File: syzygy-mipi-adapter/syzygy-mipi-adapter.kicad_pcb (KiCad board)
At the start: 4 copper layers, 45 x 70 mm, 67 parts, among them J1 Conn_02x06_Odd_Even, J10 501951-2230, J2 SYZYGY_STD, J3 Conn_01x02, J5 SM03B-SRSS-TB, J8 501951-2230, J9 501951-2230, Q1 DMG1024UV-7, Q2 DMG1024UV-7, U1 RP2350_80QFN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

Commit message: fixes
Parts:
- removed H2: MountingHole_Pad, SYZYGY:MountingHole_3.2mm_M3_6.5mm_Pad_TopBottom
- added FID1: Fiducial, Fiducial:Fiducial_0.75mm_Mask1.5mm, F.Cu at (101.8, 70.0)
- added FID2: Fiducial, Fiducial:Fiducial_0.75mm_Mask1.5mm, F.Cu at (143.2, 61.8)
- added FID3: Fiducial, Fiducial:Fiducial_0.75mm_Mask1.5mm, F.Cu at (101.8, 128.2)
- added FID4: Fiducial, Fiducial:Fiducial_0.75mm_Mask1.5mm, F.Cu at (143.2, 128.2)
- added FID5: Fiducial, Fiducial:Fiducial_0.75mm_Mask1.5mm, B.Cu at (101.8, 70.0)
- added FID6: Fiducial, Fiducial:Fiducial_0.75mm_Mask1.5mm, B.Cu at (143.2, 61.8)
- added FID7: Fiducial, Fiducial:Fiducial_0.75mm_Mask1.5mm, B.Cu at (101.8, 128.2)
- added FID8: Fiducial, Fiducial:Fiducial_0.75mm_Mask1.5mm, B.Cu at (143.2, 128.2)
- added LOGO1: SYZYGY STD logo, SYZYGY:SYZYGY_STD_Logo, F.Cu at (108.5, 63.1)
- added LOGO2: SYZYGY logo, SYZYGY:SYZYGY_Logo, F.Cu at (115.0, 62.0)
- added R20: 10K, Resistor_SMD:R_0402_1005Metric, B.Cu at (124.3, 116.8)
- added R21: 0805, Resistor_SMD:R_0805_2012Metric_Pad1.20x1.40mm_HandSolder, F.Cu at (135.6, 120.3)
- C2, R2, R8: moved to B.Cu
- J3: footprint Connector_PinHeader_1.27mm:PinHeader_1x03_P1.27mm_Vertical -> Connector_PinHeader_1.27mm:PinHeader_1x04_P1.27mm_Vertical
- U2: value W25X20CLSNIG -> W25Q32JVSSIQ
- moved C33 13.3 mm to (119.4, 110.8)
- moved J1 12.8 mm to (124.5, 124.0), turned to -90 degrees
- moved C8 10.1 mm to (121.9, 109.5)
- moved R2 7.30 mm to (119.9, 114.2), turned to 0 degrees
- moved R4 6.94 mm to (122.7, 114.8), turned to 0 degrees
- moved TP2 5.51 mm to (107.0, 116.5)
- moved C38 5.30 mm to (124.8, 114.4), turned to 0 degrees
- moved J3 5.20 mm to (140.0, 111.5)
- moved C35 4.61 mm to (124.8, 115.3), turned to 0 degrees
- moved R9 4.12 mm to (126.2, 109.1), turned to 180 degrees
- moved R8 3.71 mm to (126.2, 108.1)
- moved R7 2.82 mm to (123.3, 116.8)
- moved C2 2.62 mm to (127.2, 114.0)
- moved C42 1.94 mm to (122.1, 117.4), turned to 180 degrees
- moved R1 1.84 mm to (127.2, 116.4), turned to 180 degrees
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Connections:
- R7 pad 2: Net-(U1-GPIO46_ADC6) -> Net-(U1-GPIO45_ADC5)
- U1 pad 56: unconnected-(U1-GPIO45_ADC5-Pad56) -> Net-(U1-GPIO45_ADC5)
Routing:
- net GND: track 51.5 -> 94.4 mm, vias 76 -> 81
- net /USB_BOOTn: track 7.58 -> 18.6 mm
- net Net-(J1-Pin_5): track 23.2 -> 12.5 mm
- net Net-(U1-GPIO46_ADC6): track 3.27 -> 12.9 mm
- net Net-(J1-Pin_1): track 15.3 -> 23.4 mm, vias 0 -> 2
- net P3V3D: track 30.0 -> 37.5 mm, vias 24 -> 20
- net P5VD: track 54.1 -> 46.7 mm, vias 5 -> 6
- net PVIOD: track 61.8 -> 56.0 mm, vias 8 -> 9
- net Net-(J3-Pin_1): track 1.99 -> 7.65 mm
- net /RESETn: track 7.76 -> 13.3 mm, vias 0 -> 1
- net Net-(J3-Pin_2): track 2.02 -> 7.59 mm
- net /SDA_DNA: track 68.7 -> 64.7 mm
- net /SCL_DNA: track 68.3 -> 64.3 mm
- net Net-(J1-Pin_3): track 14.0 -> 10.2 mm
- net Net-(J1-Pin_2): track 14.9 -> 11.1 mm, vias 2 -> 0
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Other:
- outline, holes or cut-outs redrawn
- board text added: "Carrier board edge"
- board text added: "MIPI Adapter Rev 0.1"
- board text removed: "3"
- board text removed: "J1"
- board text removed: "J7"
- board text removed: "MIPI Adapter Rev FIXME"

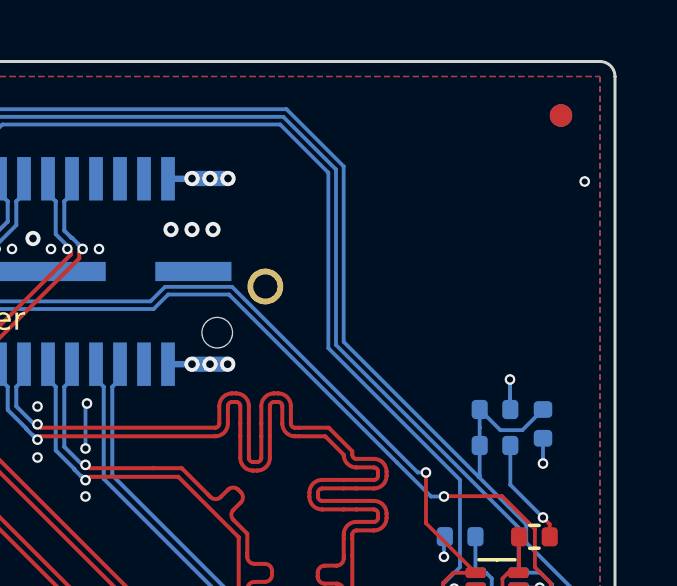
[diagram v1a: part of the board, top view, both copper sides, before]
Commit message: Restore accidentally deleted mounting hole
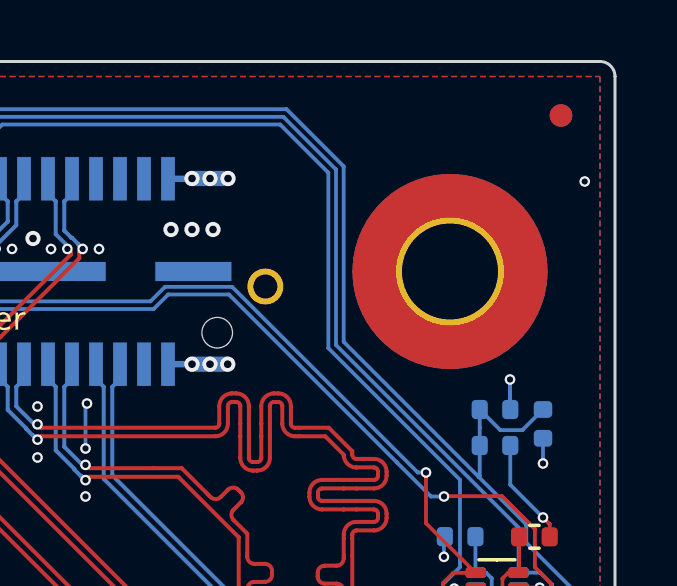
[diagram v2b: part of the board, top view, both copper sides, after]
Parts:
- added H2: MountingHole_Pad, SYZYGY:MountingHole_3.2mm_M3_6.5mm_Pad_TopBottom, F.Cu at (139.5, 67.0)
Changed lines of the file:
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@@
 	(net 157 "Net-(J3-Pin_1)")
 	(net 158 "/USB_BOOTn")
+	(net 159 "unconnected-(H2-Pad1)")
+	(net 160 "unconnected-(H2-Pad1)_1")
+	(net 161 "unconnected-(H2-Pad1)_2")
 	(footprint "SYZYGY:MountingHole_3.2mm_M3_6.5mm_Pad_TopBottom"
 		(layer "F.Cu")
@@
 		)
 	)
+	(footprint "SYZYGY:MountingHole_3.2mm_M3_6.5mm_Pad_TopBottom"
+		(layer "F.Cu")
+		(at 139.5 67)
+		(property "Reference" "H2"
+			(at 0 0.5 0)
+			(layer "F.SilkS")
+			(hide yes)
+			(effects
+				(font
+					(size 1 1)
+					(thickness 0.15)
+				)
+			)
+		)
+		(property "Value" "MountingHole_Pad"
+			(at 0 -0.5 0)
+			(layer "F.Fab")
+			(hide yes)
+			(effects
+				(font
+					(size 1 1)
+					(thickness 0.15)
+				)
+			)
+		)
+		(property "Datasheet" ""
+			(at 0 0 0)
+			(layer "F.Fab")
+			(hide yes)
+			(effects
+				(font
+					(size 1.27 1.27)
+					(thickness 0.15)
+				)
+			)
+		)
+		(property "Description" ""
+			(at 0 0 0)
+			(layer "F.Fab")
+			(hide yes)
+			(effects
+				(font
+					(size 1.27 1.27)
+					(thickness 0.15)
+				)
+			)
+		)
+		(property ki_fp_filters "MountingHole*Pad*")
+		(sheetname "/")
+		(sheetfile "syzygy-mipi-adapter.kicad_sch")
+		(attr through_hole)
+		(fp_circle
+			(center 0 0)
+			(end 3.25 0)
+			(stroke
+				(width 0.15)
+				(type solid)
+			)
+			(fill no)
+			(layer "Cmts.User")
+		)
+		(fp_circle
+			(center 0 0)
+			(end 3.5 0)
+			(stroke
+				(width 0.05)
+				(type solid)
+			)
+			(fill no)
+			(layer "F.CrtYd")
+		)
+		(pad "1" thru_hole circle
+			(at 0 0)
+			(size 3.6 3.6)
+			(drill 3.2)
+			(layers "*.Cu" "*.Mask")
+			(remove_unused_layers no)
+			(net 161 "unconnected-(H2-Pad1)_2")
+			(pinfunction "1")
+			(pintype "input+no_connect")
+		)
+		(pad "1" connect circle
+			(at 0 0)
+			(size 6.5 6.5)
+			(layers "F.Cu" "F.Mask")
+			(net 160 "unconnected-(H2-Pad1)_1")
+			(pinfunction "1")
+			(pintype "input+no_connect")
+		)
+		(pad "1" connect circle
+			(at 0 0)
+			(size 6.5 6.5)
+			(layers "B.Cu" "B.Mask")
+			(net 159 "unconnected-(H2-Pad1)")
+			(pinfunction "1")
+			(pintype "input+no_connect")
+		)
+		(embedded_fonts no)
+	)
 	(footprint "FPC:501951-2230"
 		(layer "F.Cu")
@@
 			(keep_text_aligned yes)
 		)
-		(gr_text "196.9 mils"
+		(gr_text "5.0 mm"
 			(at 95.1 126.3 90)
 			(layer "Dwgs.User")
@@
 			(keep_text_aligned yes)
 		)
-		(gr_text "236.2 mils"
+		(gr_text "6.0 mm"
 			(at 90.6 126.5 90)
 			(layer "Dwgs.User")
@@
 			(keep_text_aligned yes)
 		)
-		(gr_text "964.6 mils"
+		(gr_text "24.5 mm"
 			(at 112.25 137.95 0)
 			(layer "Dwgs.User")
@@
 			(keep_text_aligned yes)
 		)
-		(gr_text "522.060 mils"
+		(gr_text "13.260 mm"
 			(at 106.63016 50.35 0)
 			(layer "Dwgs.User")
@@
 			(keep_text_aligned yes)
 		)
-		(gr_text "355.91 mils"
+		(gr_text "9.04 mm"
 			(at 90.6 64.5 90)
 			(layer "Dwgs.User")
@@
 			(keep_text_aligned yes)
 		)
-		(gr_text "196.9 mils"
+		(gr_text "5.0 mm"
 			(at 103.4 134.3 0)
 			(layer "Dwgs.User")
@@
 			(keep_text_aligned yes)
 		)
-		(gr_text "472.4406 mils"
+		(gr_text "12.0000 mm"
 			(at 148.55 66.000005 90)
 			(layer "Dwgs.User")

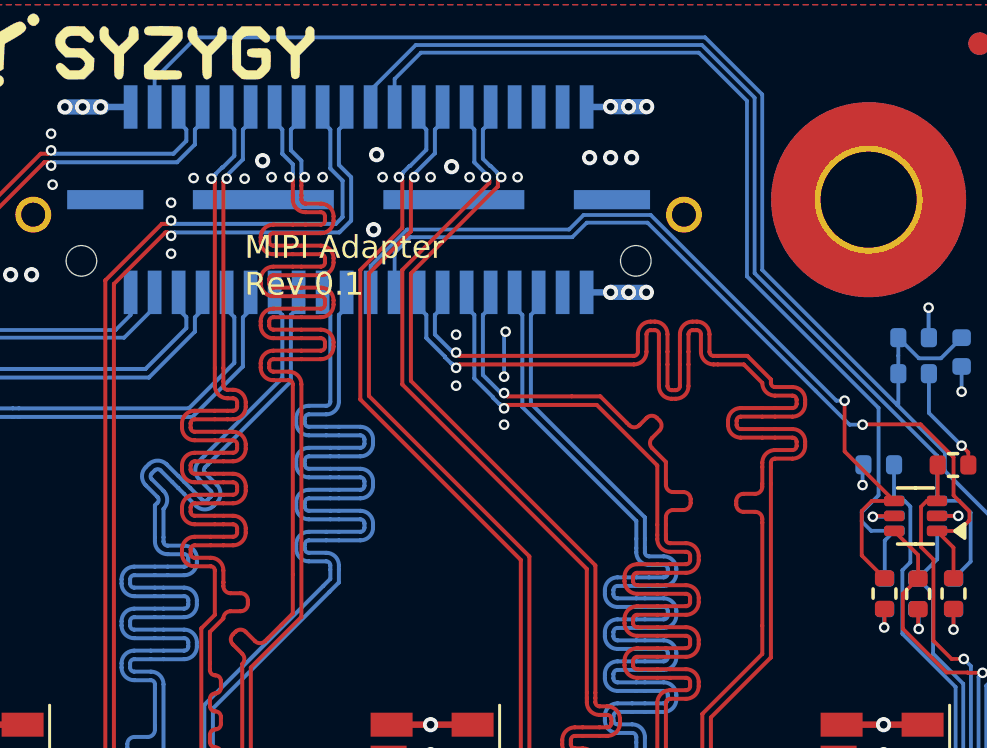
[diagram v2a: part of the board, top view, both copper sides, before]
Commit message: Fix length matching of diff pair
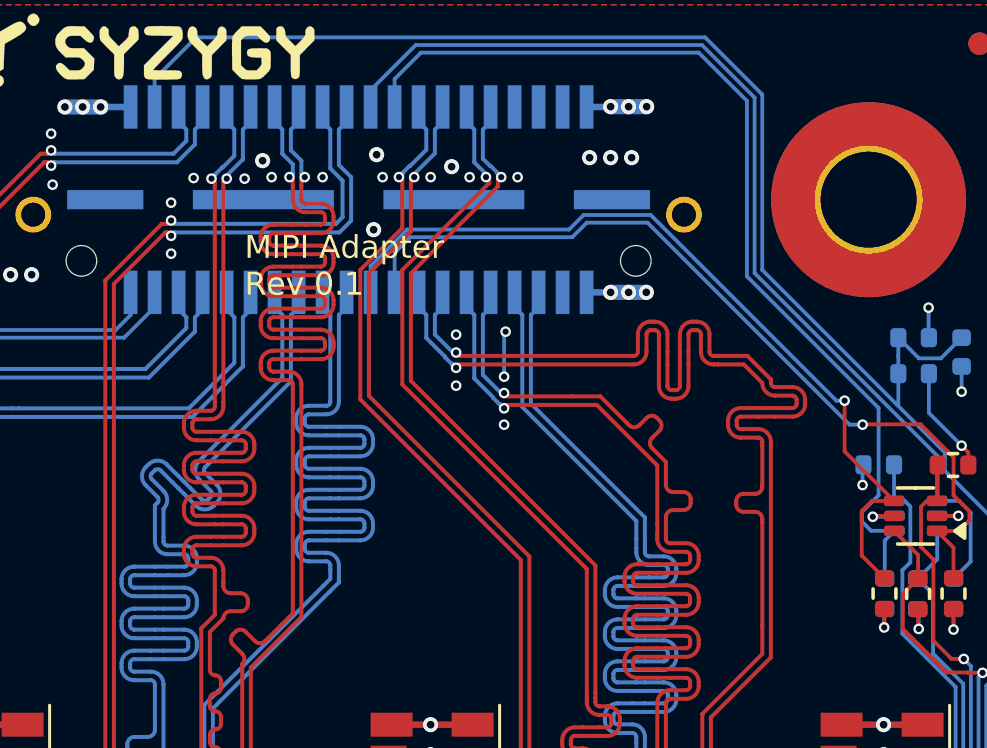
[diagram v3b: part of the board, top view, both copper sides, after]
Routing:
- net /S8P: track 44.7 -> 42.7 mm
- net /S8N: track 45.8 -> 43.7 mm
